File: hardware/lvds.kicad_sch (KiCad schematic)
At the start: 52 parts, among them U4 GateMate-CCGM1A1, Y1 ASE2-25.000MHZ-L-C-T

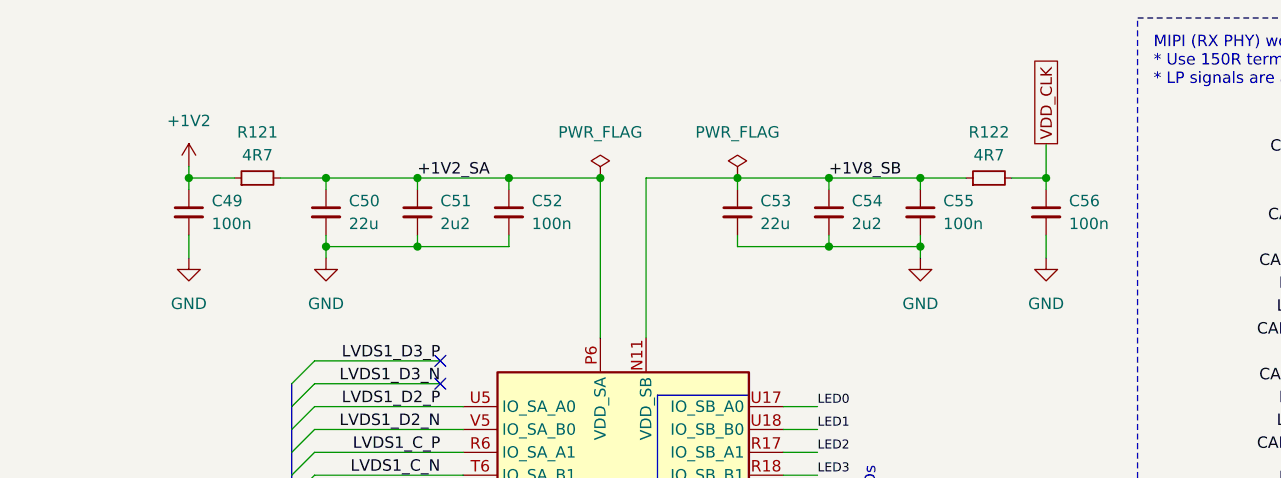
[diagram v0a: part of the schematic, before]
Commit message: power: removed rc filters from gpio domains
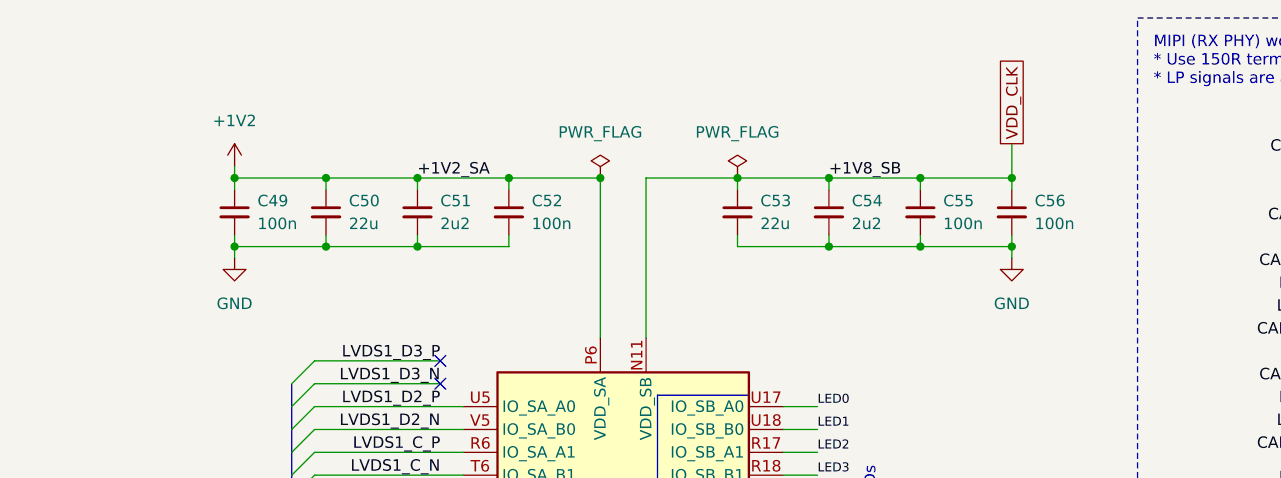
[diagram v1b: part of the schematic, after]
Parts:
- removed R121, R122: 4R7, Resistor_SMD:R_0402_1005Metric, symbol Device:R_Small
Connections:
- net +1V2_SA is gone; now on net +1V2: C50.1, C51.1, C52.1, U4.P10 (VDD_SA), U4.P6 (VDD_SA), U4.P8 (VDD_SA), U4.U6 (VDD_SA), U4.U9 (VDD_SA)
- net +1V8_SB is gone; now on net VDD_CLK: C53.1, C54.1, C55.1, U4.N11 (VDD_SB), U4.N13 (VDD_SB), U4.N18 (VDD_SB), U4.R15 (VDD_SB), U4.T18 (VDD_SB)
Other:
- moved on the sheet: C49, C56

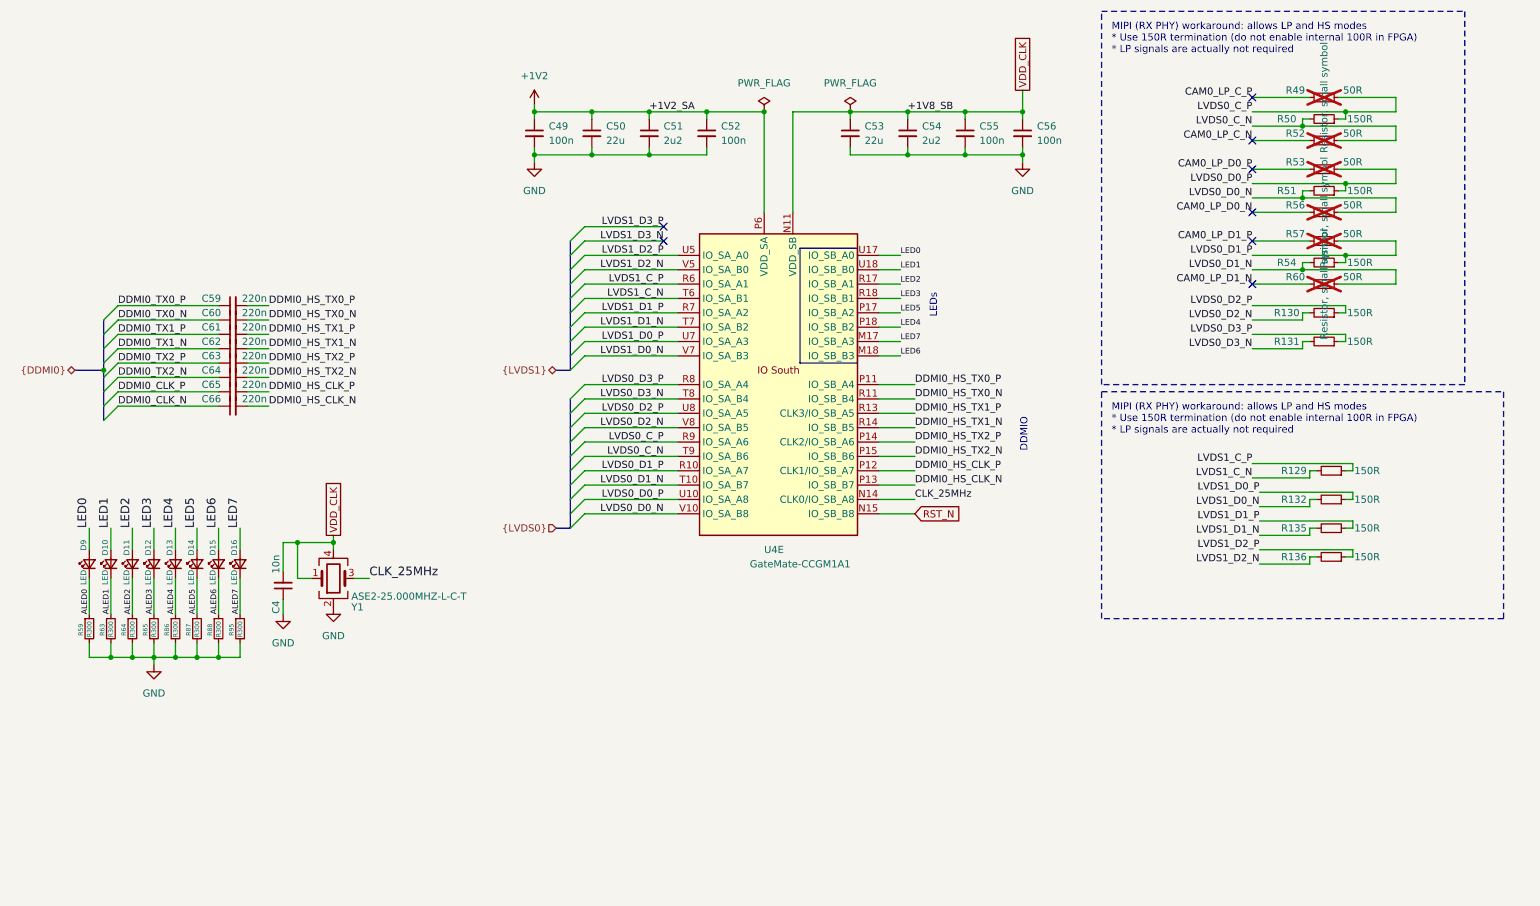
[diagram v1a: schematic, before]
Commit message: lvds: remove unused wires and components
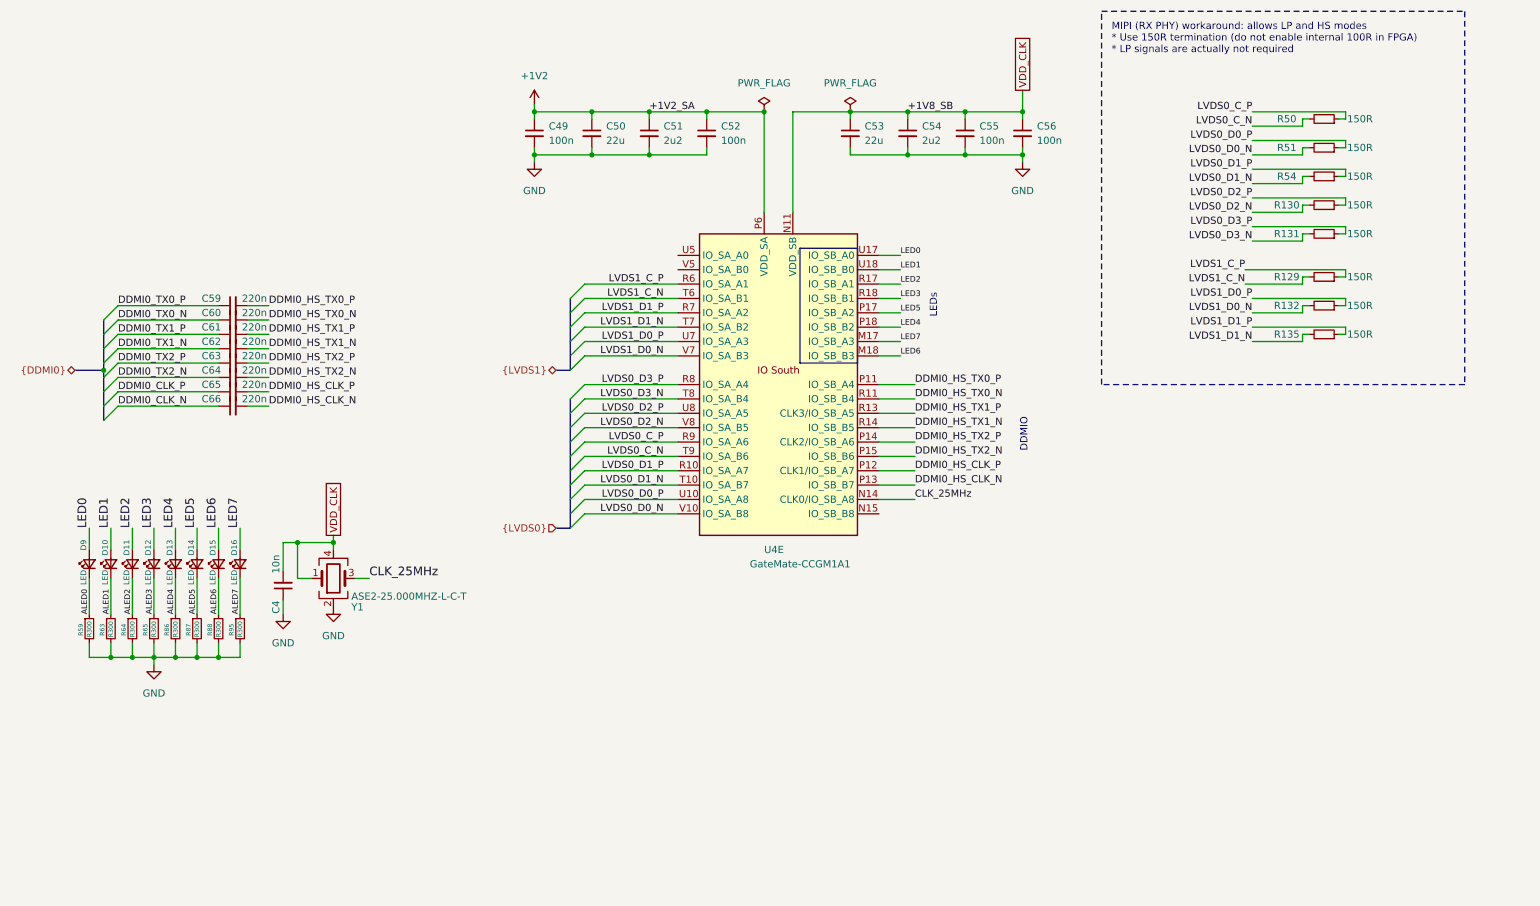
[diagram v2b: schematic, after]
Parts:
- removed R136: 150R, Resistor_SMD:R_0402_1005Metric, symbol Device:R_Small
- removed R49, R52, R53, R56, R57, R60: 50R, Resistor_SMD:R_0402_1005Metric, symbol Device:R_Small
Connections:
- net LVDS1_D2_N: no longer names the net of U4.V5 (IO_SA_B0)
- net LVDS1_D2_P: no longer names the net of U4.U5 (IO_SA_A0)
- net RST_N: no longer names the net of U4.N15 (IO_SB_B8)
- no-connect marks 8 -> 0
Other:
- moved on the sheet: R129, R130, R131, R132, R135, R51, R54

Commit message: lvds: move leds, add ddmi1
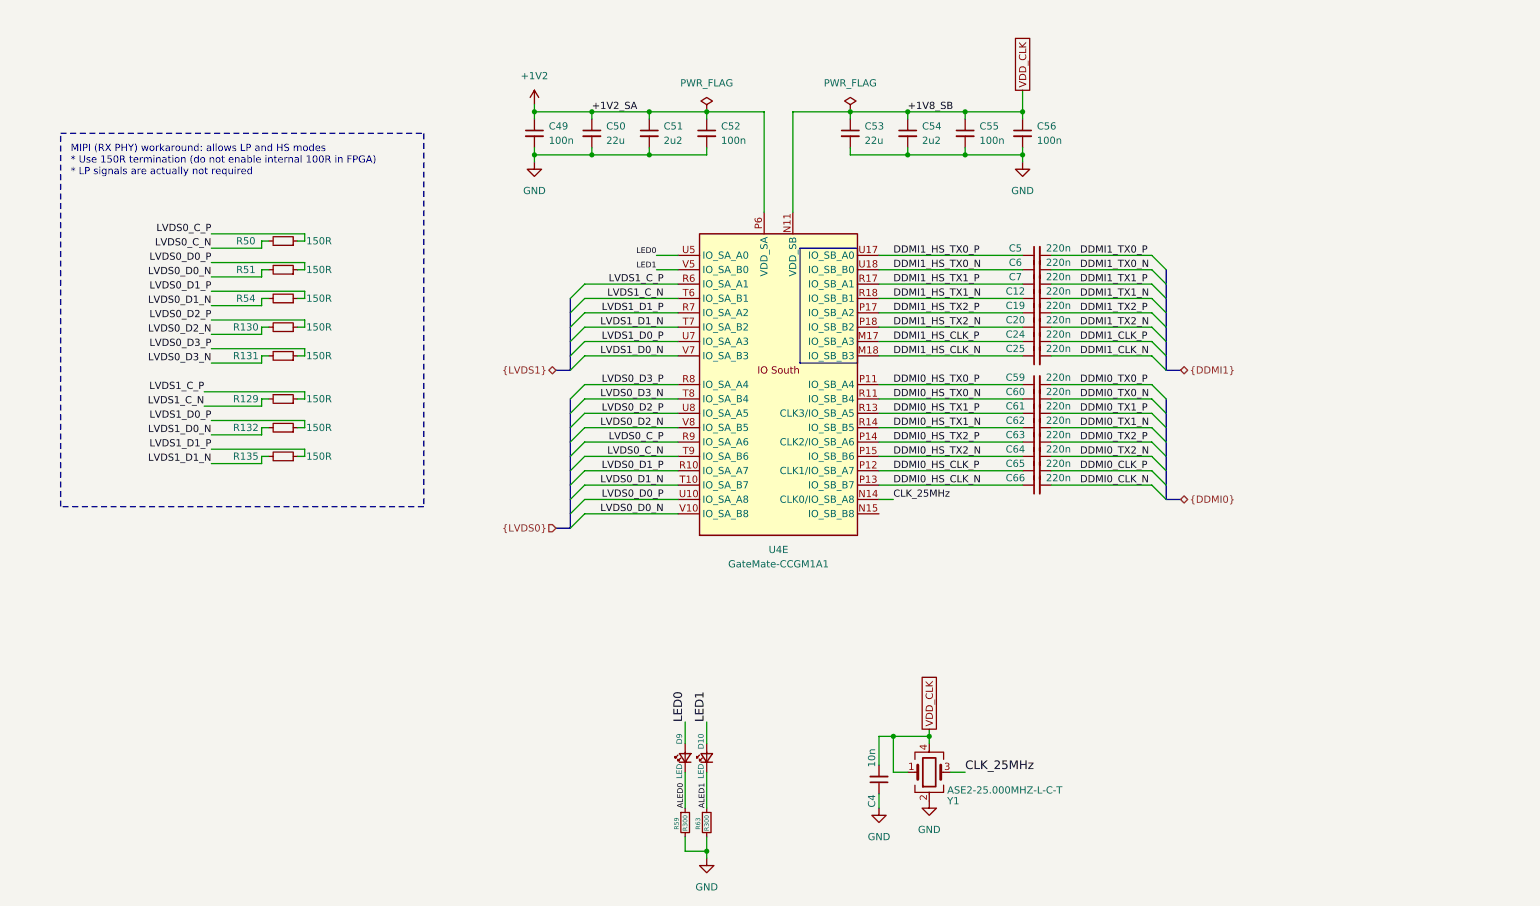
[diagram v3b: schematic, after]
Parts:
- removed D11, D12, D13, D14, D15, D16: LED, LED_SMD:LED_0603_1608Metric, symbol Device:LED_Small
- removed R64, R65, R86, R87, R88, R95: R300, Resistor_SMD:R_0402_1005Metric, symbol Device:R_Small
- added C12, C19, C20, C24, C25, C5, C6, C7: 220n, Capacitor_SMD:C_0402_1005Metric, symbol Device:C_Small
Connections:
- net DDMI0_CLK_N: now also C66.2; no longer C66.1
- net DDMI0_CLK_P: now also C65.2; no longer C65.1
- net DDMI0_HS_CLK_N: now also C66.1; no longer C66.2
- net DDMI0_HS_CLK_P: now also C65.1; no longer C65.2
- net DDMI0_HS_TX0_N: now also C60.1; no longer C60.2
- net DDMI0_HS_TX0_P: now also C59.1; no longer C59.2
- net DDMI0_HS_TX1_N: now also C62.1; no longer C62.2
- net DDMI0_HS_TX1_P: now also C61.1; no longer C61.2
- net DDMI0_HS_TX2_N: now also C64.1; no longer C64.2
- net DDMI0_HS_TX2_P: now also C63.1; no longer C63.2
- net DDMI0_TX0_N: now also C60.2; no longer C60.1
- net DDMI0_TX0_P: now also C59.2; no longer C59.1
- net DDMI0_TX1_N: now also C62.2; no longer C62.1
- net DDMI0_TX1_P: now also C61.2; no longer C61.1
- net DDMI0_TX2_N: now also C64.2; no longer C64.1
- net DDMI0_TX2_P: now also C63.2; no longer C63.1
- net LED0: now also U4.U5 (IO_SA_A0); no longer U4.U17 (IO_SB_A0)
- net LED1: now also U4.V5 (IO_SA_B0); no longer U4.U18 (IO_SB_B0)
- net LED2 renamed DDMI1_HS_TX1_P
- net DDMI1_HS_TX1_P: now also C7.1
- net LED3 renamed DDMI1_HS_TX1_N
- net DDMI1_HS_TX1_N: now also C12.1
- net LED4 renamed DDMI1_HS_TX2_N
- net DDMI1_HS_TX2_N: now also C20.1
- net LED5 renamed DDMI1_HS_TX2_P
- net DDMI1_HS_TX2_P: now also C19.1
- net LED6 renamed DDMI1_HS_CLK_N
- net DDMI1_HS_CLK_N: now also C25.1
- net LED7 renamed DDMI1_HS_CLK_P
- net DDMI1_HS_CLK_P: now also C24.1
- new net DDMI1_CLK_N: C25.2
- new net DDMI1_CLK_P: C24.2
- new net DDMI1_HS_TX0_N: C6.1, U4.U18 (IO_SB_B0)
- new net DDMI1_HS_TX0_P: C5.1, U4.U17 (IO_SB_A0)
- new net DDMI1_TX0_N: C6.2
- new net DDMI1_TX0_P: C5.2
- new net DDMI1_TX1_N: C12.2
- new net DDMI1_TX1_P: C7.2
- new net DDMI1_TX2_N: C20.2
- new net DDMI1_TX2_P: C19.2
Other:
- note removed: "DDMIO"
- note removed: "LEDs"
- moved on the sheet: C4, C59, C60, C61, C62, C63, C64, C65, C66, D10, D9, R129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

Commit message: minor schematic revisions
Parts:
- removed C4: 10n, Capacitor_SMD:C_0402_1005Metric, symbol Device:C_Small
- removed Y1: ASE2-25.000MHZ-L-C-T, Crystal:Crystal_SMD_TXC_7M-4Pin_3.2x2.5mm, symbol Device:Crystal_GND24
- R129, R130, R131, R132, R135, R50, R51, R54: value 150R -> 150
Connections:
- net CLK_25MHz: no longer names the net of U4.N14 (CLK0/IO_SB_A8)
- net VDD_CLK renamed +1V8
- no-connect marks 0 -> 2
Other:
- note removed: "MIPI (RX PHY) workaround: allows LP and HS modes * Use 150R termination (do not enable internal 100R in FPGA) * LP signals are actually not required"
- moved on the sheet: C12, C19, C20, C24, C25, C49, C5, C50, C51, C52, C53, C54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
